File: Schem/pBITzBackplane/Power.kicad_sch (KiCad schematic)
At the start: 10 parts, among them J1 ATX-24, Q1 BSS138, SW1 SW_Push, U1 ATtiny85-20P

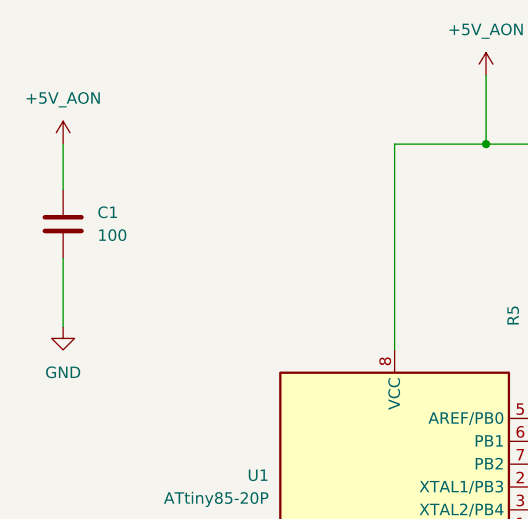
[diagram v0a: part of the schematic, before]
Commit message: Added all the manufacturer part numbers to the KiCad schematics and PCB files. This will make it easier to order the parts for the project and ensure that the correct components are used. I also removed some of the old schematics that were no longer needed, such as the BaudClock, ConsolePort, DeviceSelectDecode, GPIOUserSerial, IO Controller, UserPorts, Video, and Z80HomeBrew schematics. These changes will help to streamline the design and make it easier to understand.
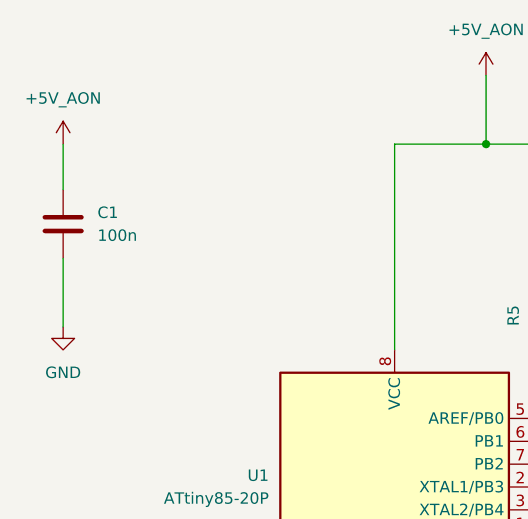
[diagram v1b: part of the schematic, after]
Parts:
- C1: value 100 -> 100n; MANUFACTURER_PART_NUMBER (none) -> C0603C104K3RACTU
- J1: MANUFACTURER_PART_NUMBER (none) -> 0039281243
- Q1: MANUFACTURER_PART_NUMBER (none) -> BSS138
- R1, R5: MANUFACTURER_PART_NUMBER (none) -> RC0603FR-0710KL
- R2, R3, R4: MANUFACTURER_PART_NUMBER (none) -> RC0603FR-074K7L
- U1: MANUFACTURER_PART_NUMBER (none) -> A 08-LC-TT
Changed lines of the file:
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@@
+			)
+		)
+		(property "MANUFACTURER_PART_NUMBER" "RC0603FR-074K7L"
+			(at 96.52 138.43 0)
+			(effects
+				(font
+					(size 1.27 1.27)
+				)
+				(hide yes)
 			)
 		)
@@
 			)
 		)
+		(property "MANUFACTURER_PART_NUMBER" "BSS138"
+			(at 139.7 115.57 90)
+			(effects
+				(font
+					(size 1.27 1.27)
+				)
+				(hide yes)
+			)
+		)
 		(pin "2"
 		)
@@
 		)
 		(property "VENDOR" ""
+			(at 87.63 101.6 90)
+			(effects
+				(font
+					(size 1.27 1.27)
+				)
+				(hide yes)
+			)
+		)
+		(property "MANUFACTURER_PART_NUMBER" "RC0603FR-0710KL"
 			(at 87.63 101.6 90)
 			(effects
@@
 			)
 		)
+		(property "MANUFACTURER_PART_NUMBER" "A 08-LC-TT"
+			(at 69.85 120.65 0)
+			(effects
+				(font
+					(size 1.27 1.27)
+				)
+				(hide yes)
+			)
+		)
 		(pin "1"
 		)
@@
 			)
 		)
+		(property "MANUFACTURER_PART_NUMBER" "RC0603FR-0710KL"
+			(at 104.14 118.11 90)
+			(effects
+				(font
+					(size 1.27 1.27)
+				)
+				(hide yes)
+			)
+		)
 		(pin "2"
 		)
@@
 			)
 		)
+		(property "MANUFACTURER_PART_NUMBER" "RC0603FR-074K7L"
+			(at 102.87 102.87 90)
+			(effects
+				(font
+					(size 1.27 1.27)
+				)
+				(hide yes)
+			)
+		)
 		(pin "2"
 		)
@@
 			)
 		)
-		(property "Value" "100"
+		(property "Value" "100n"
 			(at 36.83 92.7099 0)
 			(effects
@@
 		)
 		(property "VENDOR" ""
+			(at 33.02 91.44 0)
+			(effects
+				(font
+					(size 1.27 1.27)
+				)
+				(hide yes)
+			)
+		)
+		(property "MANUFACTURER_PART_NUMBER" "C0603C104K3RACTU"
 			(at 33.02 91.44 0)
 			(effects
@@
 			)
 		)
+		(property "MANUFACTURER_PART_NUMBER" "RC0603FR-074K7L"
+			(at 109.22 138.43 0)
+			(effects
+				(font
+					(size 1.27 1.27)
+				)
+				(hide yes)
+			)
+		)
 		(pin "2"
 		)
@@
 			(at 191.77 100.33 0)
 			(effects
+				(font
+					(size 1.27 1.27)
+				)
+				(hide yes)
+			)
+		)
+		(property "MANUFACTURER_PART_NUMBER" "0039281243"
+			(at 191.77 100.33 0)
+			(effects

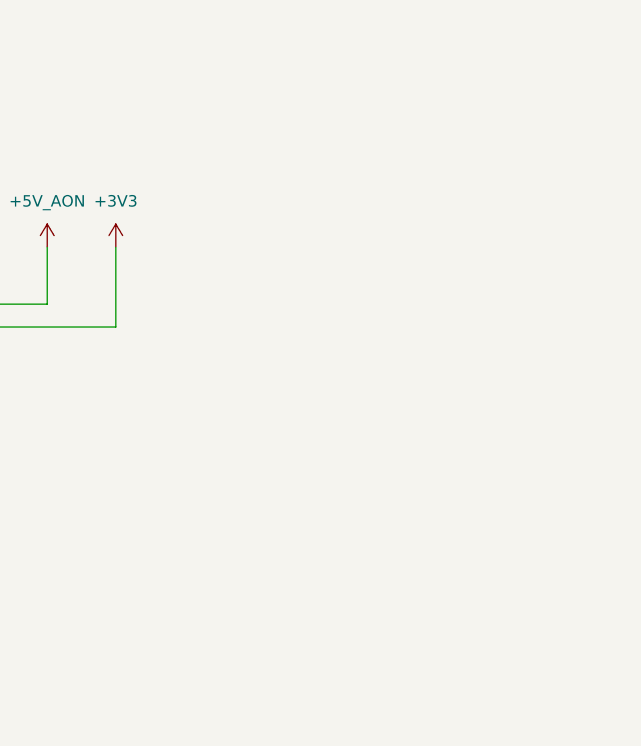
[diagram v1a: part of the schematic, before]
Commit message: Added bypass caps on power lines.
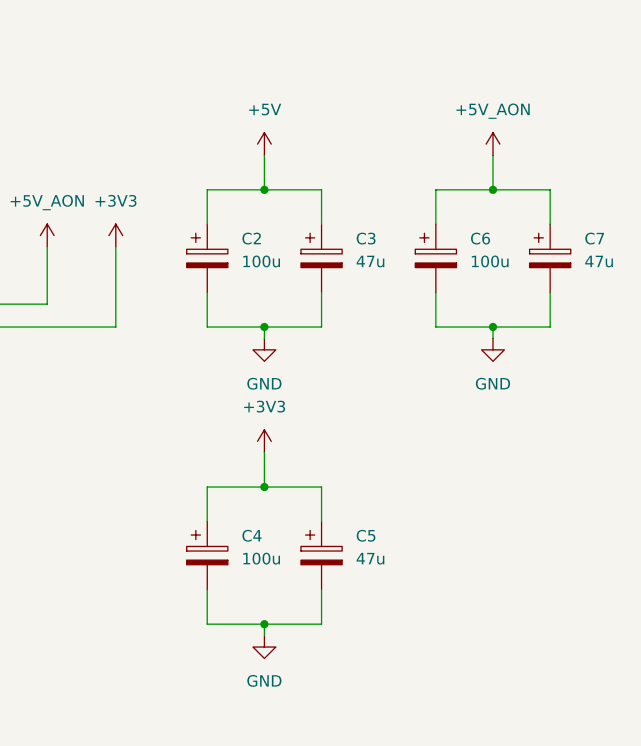
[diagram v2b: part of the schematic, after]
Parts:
- added C2, C4, C6: 100u, Capacitor_THT:CP_Radial_D5.0mm_P2.00mm, symbol Device:C_Polarized
- added C3, C5, C7: 47u, Capacitor_THT:CP_Radial_D5.0mm_P2.00mm, symbol Device:C_Polarized
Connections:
- net +3V3: now also C4.1, C5.1
- net +5V: now also C2.1, C3.1
- net +5V_AON: now also C6.1, C7.1
- net GND: now also C2.2, C3.2, C4.2, C5.2, C6.2, C7.2
